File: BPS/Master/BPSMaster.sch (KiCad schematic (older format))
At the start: 21 parts, among them J1 SWD, J13 CAN Analyzer, J5 SPI Analyzer, SW1 B3SL-1002P, U1 STM32F413RHTx, Y1 8M

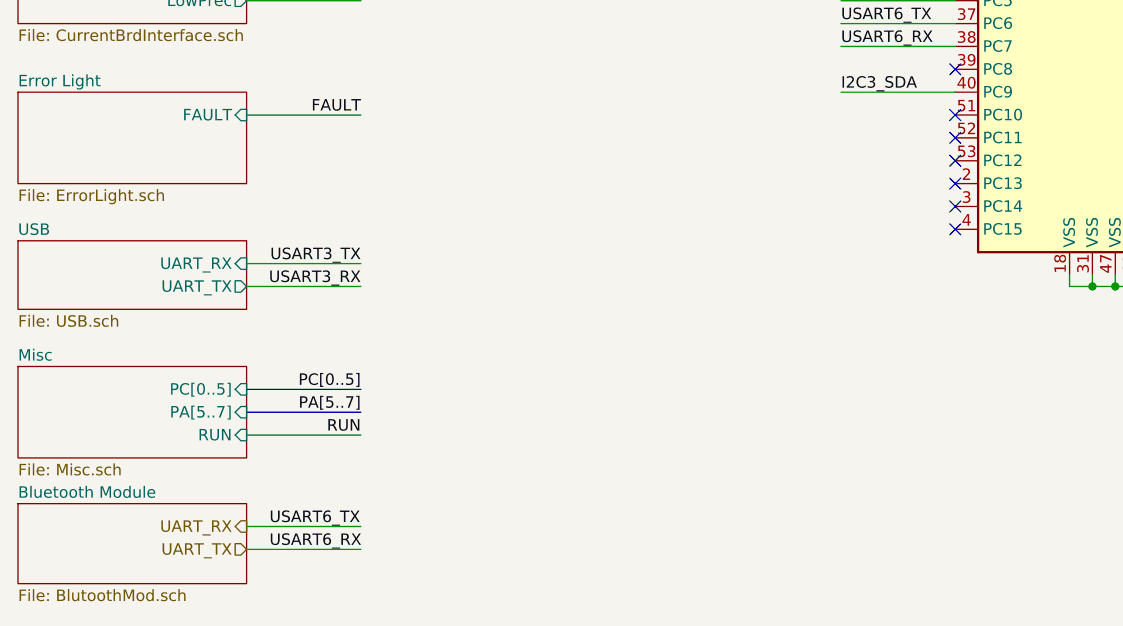
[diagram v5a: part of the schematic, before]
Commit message: Connected hierarchial sheets. Added text for all status led's.
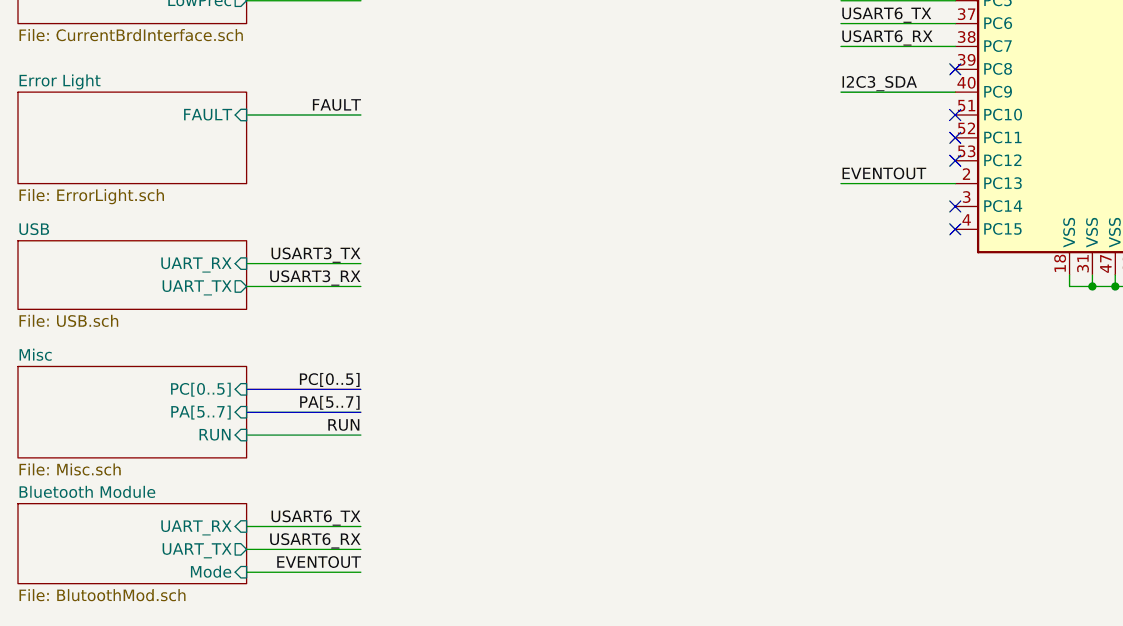
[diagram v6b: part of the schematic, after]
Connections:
- net EVENTOUT: now reaches U1.2 (PC13)
- net UART_RX renamed USART6_TX
- net UART_TX renamed USART6_RX
- no-connect marks 21 -> 20
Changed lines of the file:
@@
 NoConn ~ 5100 5500
 NoConn ~ 5100 5400
-NoConn ~ 5100 5300
 NoConn ~ 6500 4300
 NoConn ~ 6500 3900
@@
 SPI1_MOSI
 Wire Wire Line
-	5100 4600 4600 4600
-Wire Wire Line
 	5100 4700 4600 4700
-Text Label 4600 4600 0    50   ~ 0
-USART6_TX
 Text Label 4600 4700 0    50   ~ 0
 USART6_RX
@@
 F0 "Bluetooth Module" 50
 F1 "BlutoothMod.sch" 50
-$EndSheet
-Text HLabel 2000 6800 0    50   Output ~ 0
-UART_RX
-Text HLabel 2000 6900 0    50   Input ~ 0
-UART_TX
+F2 "UART_RX" I R 2000 6800 50
+F3 "UART_TX" O R 2000 6900 50
+F4 "Mode" I R 2000 7000 50
+$EndSheet
 Wire Wire Line
 	2000 6900 2500 6900
-Text Label 2100 6800 0    50   ~ 0
+Wire Wire Line
+	2000 6800 2500 6800
+Wire Wire Line
+	2000 7000 2500 7000
+Text Label 2500 6900 2    50   ~ 0
+USART6_RX
+Text Label 2500 6800 2    50   ~ 0
 USART6_TX
-Text Label 2100 6900 0    50   ~ 0
-USART6_RX
-Wire Wire Line
-	2000 6800 2500 6800
+Wire Wire Line
+	5100 5300 4600 5300
+Text Label 4600 5300 0    50   ~ 0
+EVENTOUT
+Text Label 2500 7000 2    50   ~ 0
+EVENTOUT
 Wire Bus Line
 	7100 2700 7100 3000
 Wire Bus Line
 	4500 3800 4500 4300
+Wire Wire Line
+	5100 4600 4600 4600
+Text Label 4600 4600 0    50   ~ 0
+USART6_TX
 $EndSCHEMATC

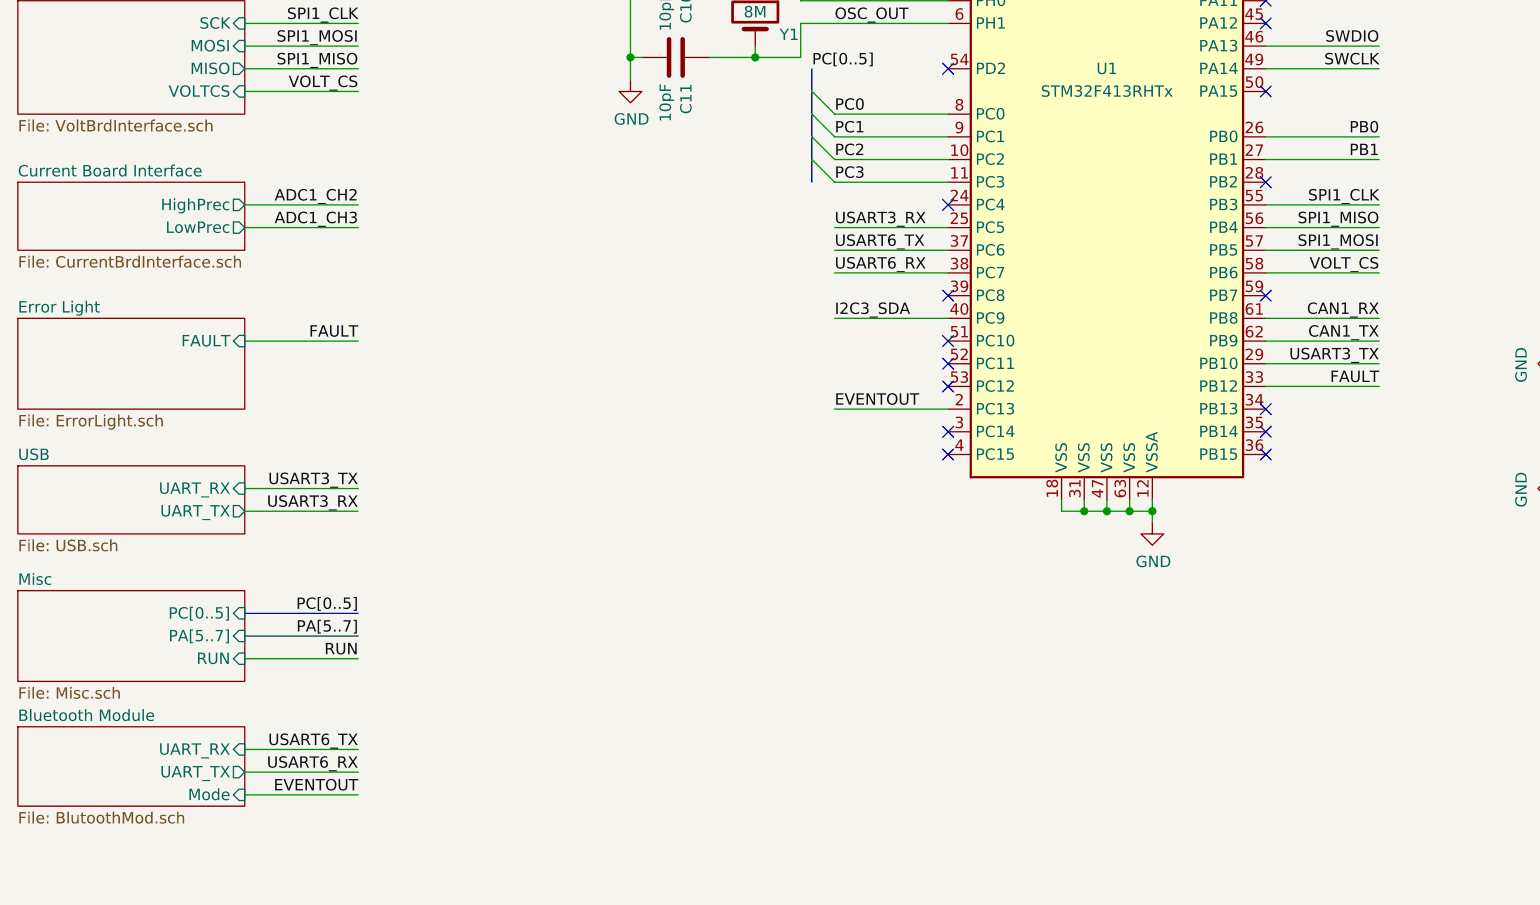
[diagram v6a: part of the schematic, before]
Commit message: Added PWM for fan control. Since max output of pins are 3V, used buttons to connect 12V to fan. Used pin 28 of STM for PWM using Low Power Timer 1.
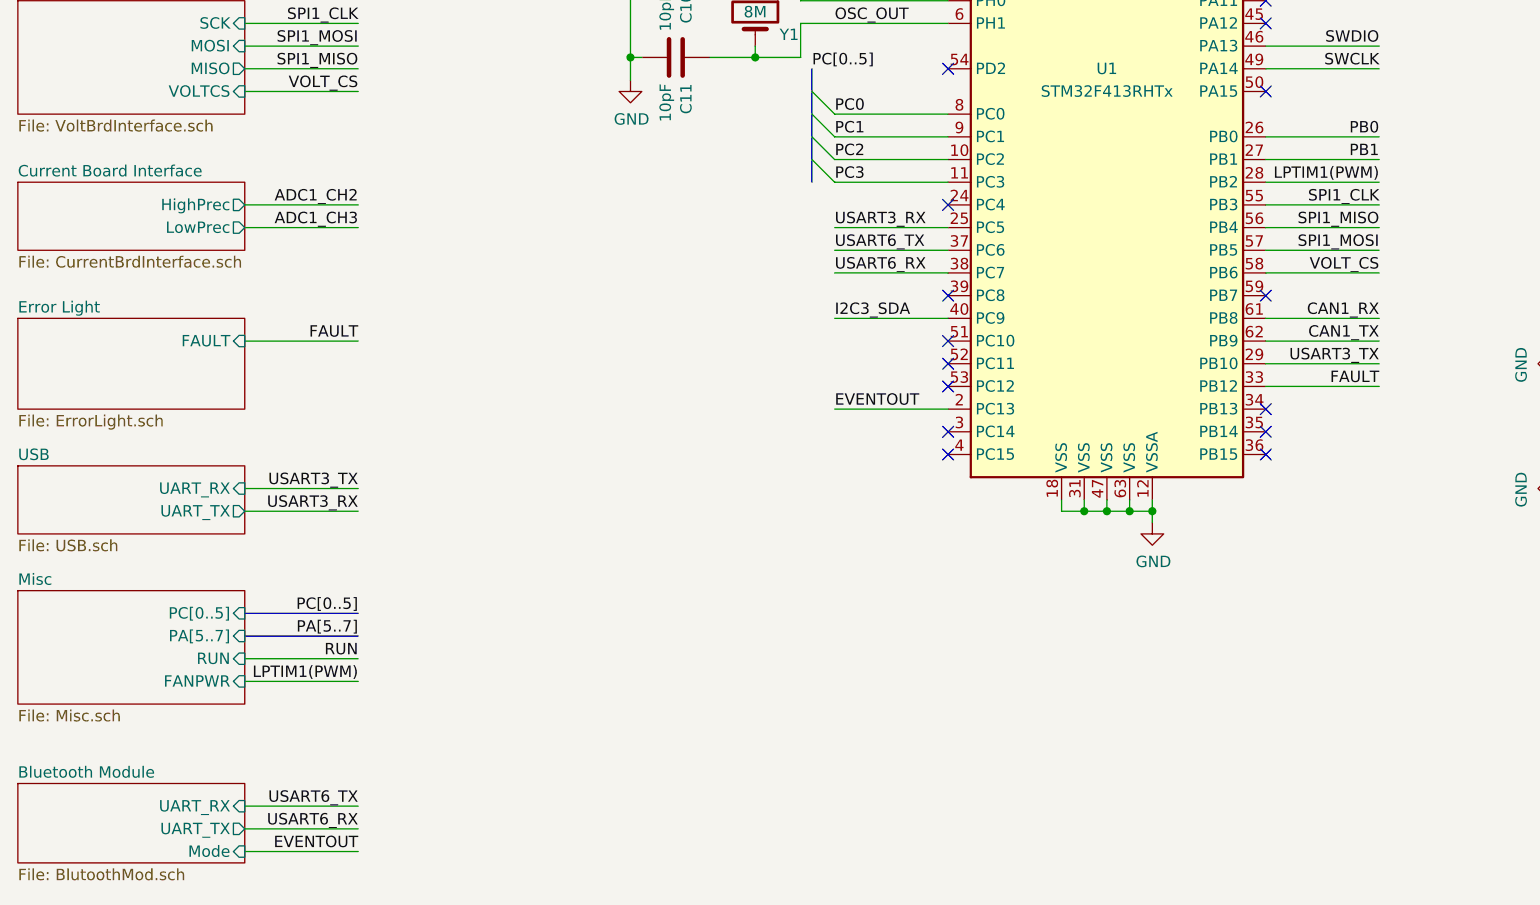
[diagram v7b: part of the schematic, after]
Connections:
- net LPTIM1(PWM): now reaches U1.28 (PB2)
- no-connect marks 20 -> 19
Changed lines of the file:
@@
 	10550 2900 10650 2900
 $Sheet
-S 1000 6100 1000 400
+S 1000 6100 1000 500
 U 5C392C6A
 F0 "Misc" 50
@@
 F3 "PA[5..7]" I R 2000 6300 50
 F4 "RUN" I R 2000 6400 50
+F5 "FANPWR" I R 2000 6500 50
 $EndSheet
 Text Notes 8650 1150 0    100  ~ 20
@@
 NoConn ~ 5100 5500
 NoConn ~ 5100 5400
-NoConn ~ 6500 4300
 NoConn ~ 6500 3900
 NoConn ~ 5100 3800
@@
 USART6_RX
 $Sheet
-S 1000 6700 1000 350
+S 1000 6950 1000 350
 U 5EE39517
 F0 "Bluetooth Module" 50
 F1 "BlutoothMod.sch" 50
-F2 "UART_RX" I R 2000 6800 50
-F3 "UART_TX" O R 2000 6900 50
-F4 "Mode" I R 2000 7000 50
-$EndSheet
-Wire Wire Line
-	2000 6900 2500 6900
-Wire Wire Line
-	2000 6800 2500 6800
-Wire Wire Line
-	2000 7000 2500 7000
-Text Label 2500 6900 2    50   ~ 0
+F2 "UART_RX" I R 2000 7050 50
+F3 "UART_TX" O R 2000 7150 50
+F4 "Mode" I R 2000 7250 50
+$EndSheet
+Wire Wire Line
+	2000 7150 2500 7150
+Wire Wire Line
+	2000 7050 2500 7050
+Wire Wire Line
+	2000 7250 2500 7250
+Text Label 2500 7150 2    50   ~ 0
 USART6_RX
-Text Label 2500 6800 2    50   ~ 0
+Text Label 2500 7050 2    50   ~ 0
 USART6_TX
 Wire Wire Line
@@
 Text Label 4600 5300 0    50   ~ 0
 EVENTOUT
-Text Label 2500 7000 2    50   ~ 0
+Text Label 2500 7250 2    50   ~ 0
 EVENTOUT
+Wire Wire Line
+	5100 4600 4600 4600
+Text Label 4600 4600 0    50   ~ 0
+USART6_TX
+Wire Wire Line
+	6500 4300 7000 4300
+Text Label 7000 4300 2    50   ~ 0
+LPTIM1(PWM)
+Wire Wire Line
+	2000 6500 2500 6500
 Wire Bus Line
 	7100 2700 7100 3000
 Wire Bus Line
 	4500 3800 4500 4300
-Wire Wire Line
-	5100 4600 4600 4600
-Text Label 4600 4600 0    50   ~ 0
-USART6_TX
+Text Label 2500 6500 2    50   ~ 0
+LPTIM1(PWM)
 $EndSCHEMATC

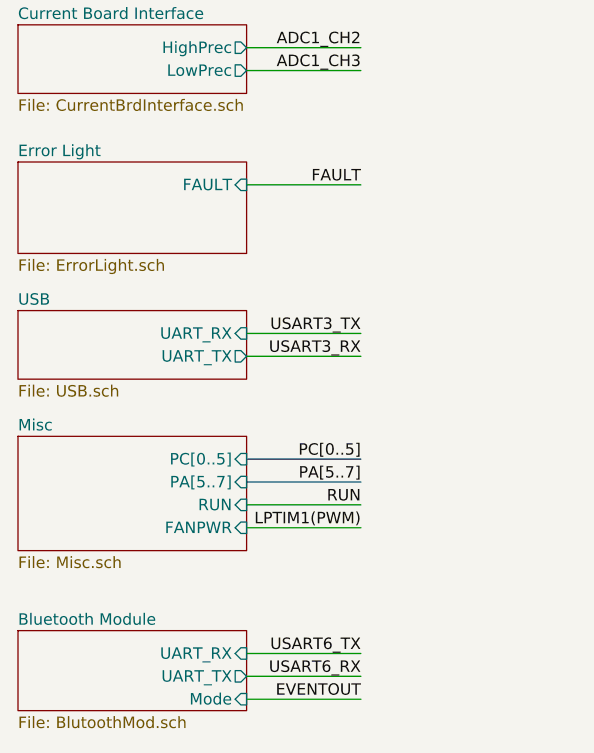
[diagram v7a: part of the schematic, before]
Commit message: Added UART_TX indicator light.
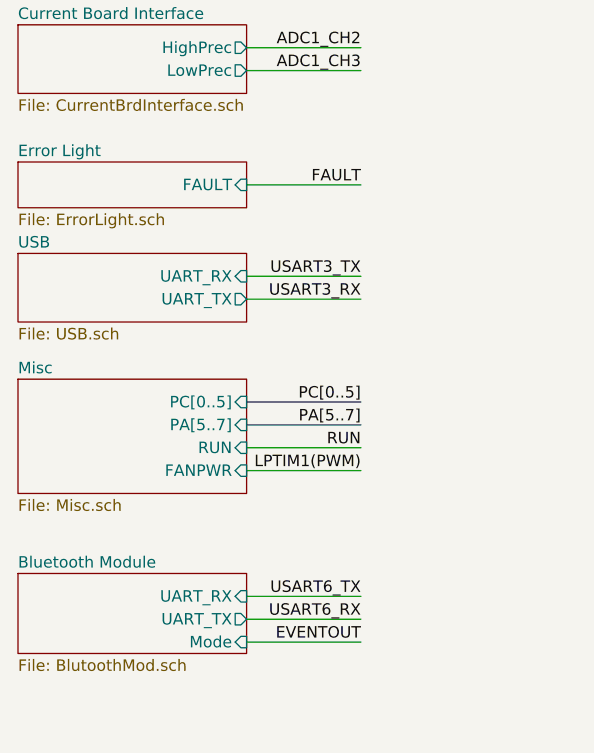
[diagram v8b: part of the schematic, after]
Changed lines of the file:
@@
 	10550 2900 10650 2900
 $Sheet
-S 1000 6100 1000 500
+S 1000 5850 1000 500
 U 5C392C6A
 F0 "Misc" 50
 F1 "Misc.sch" 50
-F2 "PC[0..5]" I R 2000 6200 50
-F3 "PA[5..7]" I R 2000 6300 50
-F4 "RUN" I R 2000 6400 50
-F5 "FANPWR" I R 2000 6500 50
+F2 "PC[0..5]" I R 2000 5950 50
+F3 "PA[5..7]" I R 2000 6050 50
+F4 "RUN" I R 2000 6150 50
+F5 "FANPWR" I R 2000 6250 50
 $EndSheet
 Text Notes 8650 1150 0    100  ~ 20
@@
 Text Label 4500 3800 0    50   ~ 0
 PC[0..5]
-Text Label 2500 6200 2    50   ~ 0
+Text Label 2500 5950 2    50   ~ 0
 PC[0..5]
 Wire Wire Line
@@
 PA[5..7]
 Wire Bus Line
-	2000 6200 2500 6200
+	2000 5950 2500 5950
 Wire Bus Line
-	2000 6300 2500 6300
-Text Label 2500 6300 2    50   ~ 0
+	2000 6050 2500 6050
+Text Label 2500 6050 2    50   ~ 0
 PA[5..7]
 $Comp
@@
 RUN
 Wire Wire Line
-	2000 6400 2500 6400
-Text Label 2500 6400 2    50   ~ 0
+	2000 6150 2500 6150
+Text Label 2500 6150 2    50   ~ 0
 RUN
 Wire Wire Line
@@
 $EndSheet
 $Sheet
-S 1000 4900 1000 400
+S 1000 4900 1000 200
 U 5D923D59
 F0 "Error Light" 50
@@
 ADC1_CH3
 $Sheet
-S 1000 5550 1000 300
+S 1000 5300 1000 300
 U 5D99F192
 F0 "USB" 50
 F1 "USB.sch" 50
-F2 "UART_RX" I R 2000 5650 50
-F3 "UART_TX" O R 2000 5750 50
-$EndSheet
-Text Label 2500 5650 2    50   ~ 0
+F2 "UART_RX" I R 2000 5400 50
+F3 "UART_TX" O R 2000 5500 50
+$EndSheet
+Text Label 2500 5400 2    50   ~ 0
 USART3_TX
 Wire Wire Line
-	2000 5650 2500 5650
-Text Label 2500 5750 2    50   ~ 0
+	2000 5400 2500 5400
+Text Label 2500 5500 2    50   ~ 0
 USART3_RX
 Wire Wire Line
-	2000 5750 2500 5750
+	2000 5500 2500 5500
 $Comp
 L power:GND #PWR0101
@@
 USART6_RX
 $Sheet
-S 1000 6950 1000 350
+S 1000 6700 1000 350
 U 5EE39517
 F0 "Bluetooth Module" 50
 F1 "BlutoothMod.sch" 50
-F2 "UART_RX" I R 2000 7050 50
-F3 "UART_TX" O R 2000 7150 50
-F4 "Mode" I R 2000 7250 50
-$EndSheet
-Wire Wire Line
-	2000 7150 2500 7150
-Wire Wire Line
-	2000 7050 2500 7050
-Wire Wire Line
-	2000 7250 2500 7250
-Text Label 2500 7150 2    50   ~ 0
+F2 "UART_RX" I R 2000 6800 50
+F3 "UART_TX" O R 2000 6900 50
+F4 "Mode" I R 2000 7000 50
+$EndSheet
+Wire Wire Line
+	2000 6900 2500 6900
+Wire Wire Line
+	2000 6800 2500 6800
+Wire Wire Line
+	2000 7000 2500 7000
+Text Label 2500 6900 2    50   ~ 0
 USART6_RX
-Text Label 2500 7050 2    50   ~ 0
+Text Label 2500 6800 2    50   ~ 0
 USART6_TX
 Wire Wire Line
@@
 Text Label 4600 5300 0    50   ~ 0
 EVENTOUT
-Text Label 2500 7250 2    50   ~ 0
+Text Label 2500 7000 2    50   ~ 0
 EVENTOUT
 Wire Wire Line
@@
 LPTIM1(PWM)
 Wire Wire Line
-	2000 6500 2500 6500
+	2000 6250 2500 6250
+Text Label 2500 6250 2    50   ~ 0
+LPTIM1(PWM)
 Wire Bus Line
 	7100 2700 7100 3000
 Wire Bus Line
 	4500 3800 4500 4300
-Text Label 2500 6500 2    50   ~ 0
-LPTIM1(PWM)
 $EndSCHEMATC
